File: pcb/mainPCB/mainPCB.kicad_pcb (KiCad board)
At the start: 2 copper layers, 1 part, among them U1 ESP32-S3-DevKitC

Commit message: oskur, cette personne fait sûrement n'imp mais ne s'en aperçois même pas (découvrez son histoire)
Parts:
- added J1: Conn_01x30, Chris:FPC_30_Dell_0.8mm_no0, F.Cu at (102.0, 156.8)
- added J2: Conn_02x15_Counter_Clockwise, Connector_PinHeader_2.54mm:PinHeader_2x15_P2.54mm_Vertical, F.Cu at (84.4, 141.7)
- moved U1 52.6 mm to (149.1, 57.9)
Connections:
- U1 pad 5: unconnected-(U1-GPIO5/ADC1_CH4-Pad5) -> Net-(J1-Pin_14)

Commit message: wip: starting pcb wiring
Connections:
- net Net-(J1-Pin_10) renamed P10
- net Net-(J1-Pin_11) renamed P11
- net Net-(J1-Pin_12) renamed P12
- net Net-(J1-Pin_13) renamed P13
- net Net-(J1-Pin_15) renamed P15
- net Net-(J1-Pin_16) renamed P16
- net Net-(J1-Pin_17) renamed P17
- net Net-(J1-Pin_18) renamed P18
- net Net-(J1-Pin_19) renamed P19
- net Net-(J1-Pin_2) renamed P02
- net Net-(J1-Pin_20) renamed P20
- net Net-(J1-Pin_21) renamed P21
- net Net-(J1-Pin_22) renamed P22
- net Net-(J1-Pin_23) renamed P23
- net Net-(J1-Pin_24) renamed P24
- net Net-(J1-Pin_25) renamed P25
- net Net-(J1-Pin_26) renamed P26
- net Net-(J1-Pin_27) renamed P27
- net Net-(J1-Pin_28) renamed P28
- net Net-(J1-Pin_29) renamed P29
- net Net-(J1-Pin_3) renamed P03
- net Net-(J1-Pin_30) renamed P30
- net Net-(J1-Pin_4) renamed P04
- net Net-(J1-Pin_5) renamed P05
- net Net-(J1-Pin_6) renamed P06
- net Net-(J1-Pin_7) renamed P07
- net Net-(J1-Pin_8) renamed P08
- net Net-(J1-Pin_9) renamed P09
- J1 pad 1: Net-(J1-Pin_1) -> P01
- J1 pad 14: Net-(J1-Pin_14) -> P14
- J2 pad 1: Net-(J1-Pin_1) -> P01
- J2 pad 14: Net-(J1-Pin_14) -> P14
- U1 pad 22: Net-(U1-GND-Pad22) -> P01
- U1 pad 23: Net-(U1-GND-Pad22) -> P01
- U1 pad 24: Net-(U1-GND-Pad22) -> P01
- U1 pad 44: Net-(U1-GND-Pad22) -> P01
- U1 pad 5: Net-(J1-Pin_14) -> unconnected-(U1-GPIO5/ADC1_CH4-Pad5)

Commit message: wip: starting no crossing cable
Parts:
- added R1: 220, Resistor_THT:R_Axial_DIN0207_L6.3mm_D2.5mm_P10.16mm_Horizontal, F.Cu at (161.0, 116.8)
- moved J1 73.4 mm to (125.2, 87.2)
- moved J2 72.9 mm to (106.0, 72.1)
- moved U1 25.1 mm to (156.5, 81.9), turned to 90 degrees
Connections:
- net P01 renamed P01_GND
- net P02 renamed P02_unused
- net P03 renamed P03_unused
- net P04 renamed P04_CAP_LED
- net P05 renamed P05_O10
- net P06 renamed P06_O11
- net P07 renamed P07_O9
- net P08 renamed P08_O14
- net P09 renamed P09_O13
- net P10 renamed P10_O15
- net P11 renamed P11_O16
- net P12 renamed P12_O12
- net P13 renamed P13_O0
- net P14 renamed P14_O2
- net P15 renamed P15_O1
- net P16 renamed P16_O3
- net P17 renamed P17_O8
- net P18 renamed P18_O6
- net P19 renamed P19_O7
- net P20 renamed P20_O4
- net P21 renamed P21_O5
- net P23 renamed P23_I3
- net P25 renamed P25_I5
- net P27 renamed P27_I4
- net P29 renamed P29_I7
- net P30 renamed P30_unused_kb_det
- J1 pad 22: P22 -> P22_I0
- J1 pad 24: P24 -> P24_I1
- J1 pad 26: P26 -> P26_I2
- J1 pad 28: P28 -> P28_I6
- J2 pad 22: P22 -> P22_I0
- J2 pad 24: P24 -> P24_I1
- J2 pad 26: P26 -> P26_I2
- J2 pad 28: P28 -> P28_I6
- U1 pad 27: unconnected-(U1-GPIO21-Pad27) -> Net-(U1-GPIO21)
- U1 pad 38: unconnected-(U1-GPIO41/MTDI-Pad38) -> P22_I0
- U1 pad 39: unconnected-(U1-GPIO42/MTMS-Pad39) -> P24_I1
- U1 pad 40: unconnected-(U1-GPIO2/ADC1_CH1-Pad40) -> P26_I2
- U1 pad 41: unconnected-(U1-GPIO1/ADC1_CH0-Pad41) -> P28_I6

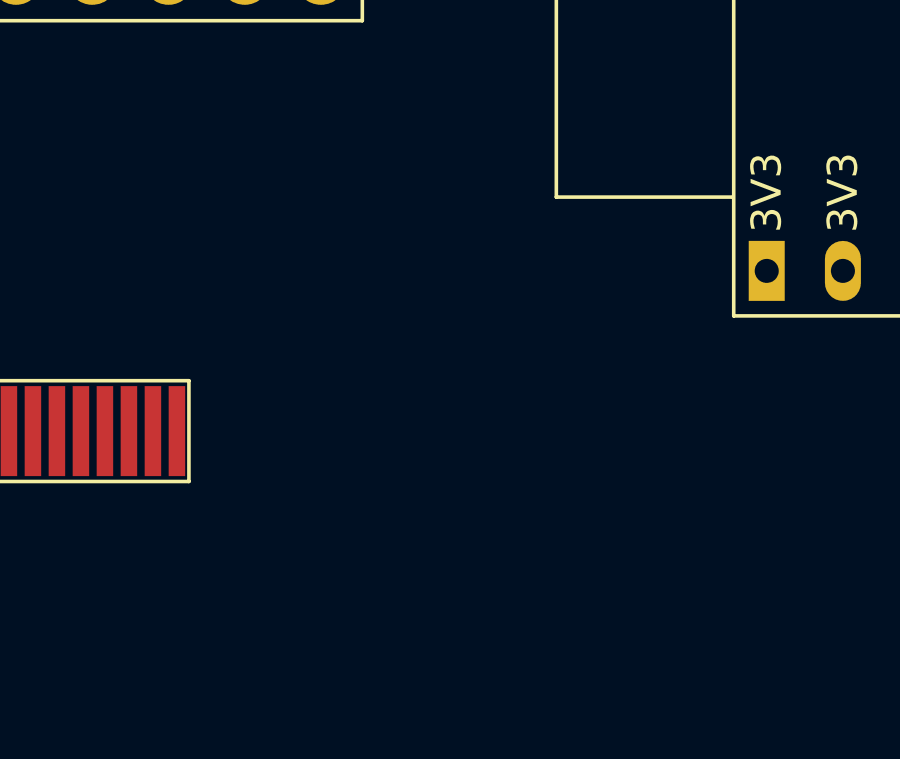
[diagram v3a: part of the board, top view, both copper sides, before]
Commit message: chore: adding backlight connectors
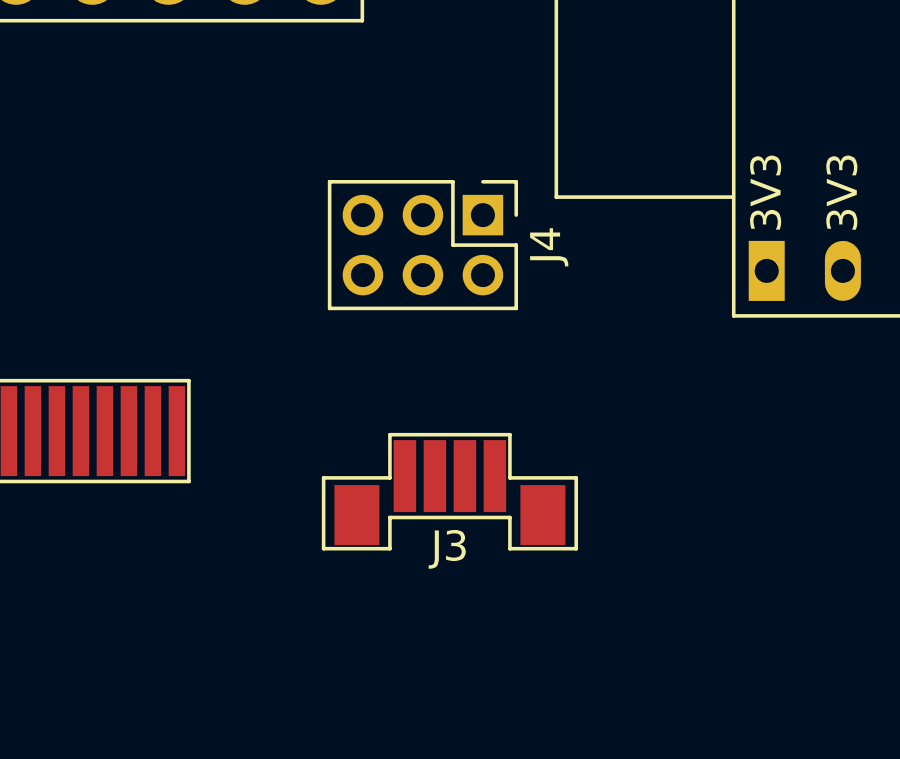
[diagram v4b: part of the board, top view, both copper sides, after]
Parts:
- added J3: Conn_01x04_Shielded_Backlight, Chris:FPC_4_Dell_1mm_with0, F.Cu at (145.9, 88.7)
- added J4: Conn_02x03_Odd_Even_Backlight, Connector_PinHeader_2.00mm:PinHeader_2x03_P2.00mm_Vertical, F.Cu at (147.0, 80.0)

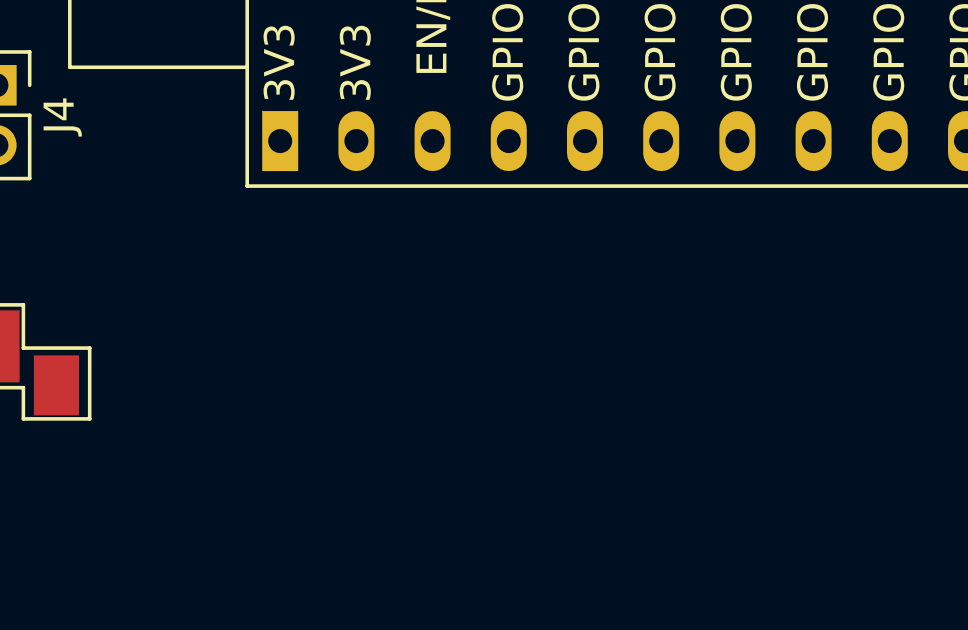
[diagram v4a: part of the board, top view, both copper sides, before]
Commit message: feat: adding NPN for caps led
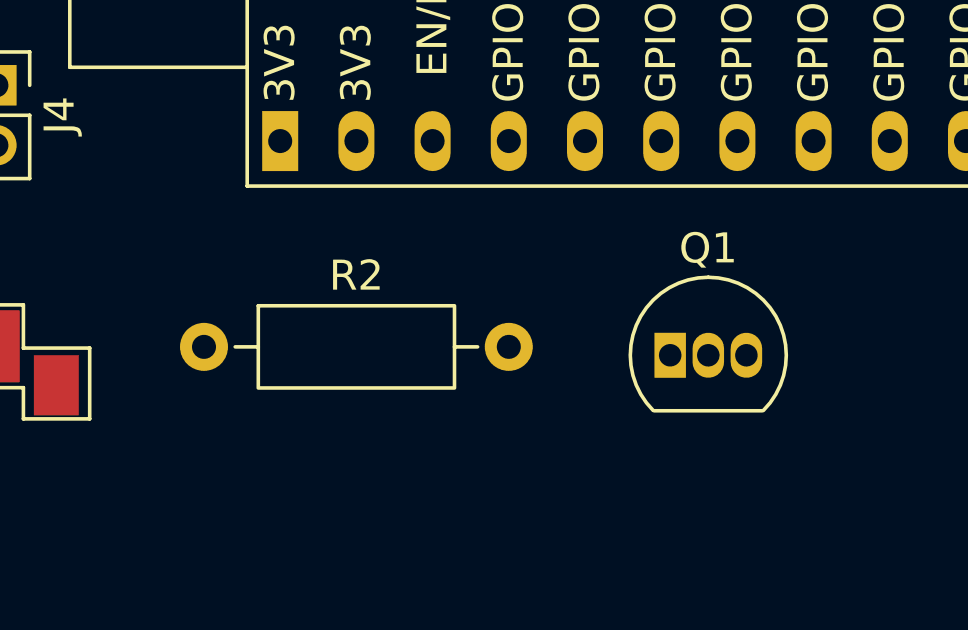
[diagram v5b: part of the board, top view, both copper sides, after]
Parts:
- added Q1: BC547, Package_TO_SOT_THT:TO-92_Inline, F.Cu at (169.5, 89.0)
- added R2: 220, Resistor_THT:R_Axial_DIN0207_L6.3mm_D2.5mm_P10.16mm_Horizontal, F.Cu at (153.9, 88.7)
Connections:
- net Net-(U1-3V3-Pad1) renamed 3_3V
- J3 pad 1: Net-(J3-Pin_1) -> P01_GND
- J4 pad 2: Net-(J3-Pin_1) -> P01_GND
- R1 pad 2: Net-(U1-GPIO21) -> Net-(Q1-E)
- U1 pad 27: Net-(U1-GPIO21) -> unconnected-(U1-GPIO21-Pad27)
- U1 pad 32: unconnected-(U1-GPIO35-Pad32) -> P14_O2
- U1 pad 33: unconnected-(U1-GPIO36-Pad33) -> P14_O2
- U1 pad 34: unconnected-(U1-GPIO37-Pad34) -> P16_O3
- U1 pad 35: unconnected-(U1-GPIO38-Pad35) -> P18_O6
- U1 pad 37: unconnected-(U1-GPIO40/MTDO-Pad37) -> P20_O4

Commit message: chore: more cables
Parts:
- J1: value Conn_01x30 -> Conn_01x30_Keyboard
- moved R1 63.1 mm to (129.8, 62.0)
- moved Q1 37.5 mm to (143.5, 62.0)
- moved U1 1.18 mm to (155.7, 81.0)
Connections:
- U1 pad 10: unconnected-(U1-GPIO17/ADC2_CH6-Pad10) -> P13_O0
- U1 pad 11: unconnected-(U1-GPIO18/ADC2_CH7-Pad11) -> P15_O1
- U1 pad 12: unconnected-(U1-GPIO8/ADC1_CH7-Pad12) -> P17_O8
- U1 pad 4: unconnected-(U1-GPIO4/ADC1_CH3-Pad4) -> CMD_CAP_LED
- U1 pad 5: unconnected-(U1-GPIO5/ADC1_CH4-Pad5) -> P05_O10
- U1 pad 6: unconnected-(U1-GPIO6/ADC1_CH5-Pad6) -> P07_O9
- U1 pad 7: unconnected-(U1-GPIO7/ADC1_CH6-Pad7) -> P09_O13
- U1 pad 8: unconnected-(U1-GPIO15/ADC2_CH4/32K_P-Pad8) -> P09_O13
- U1 pad 9: unconnected-(U1-GPIO16/ADC2_CH5/32K_N-Pad9) -> P11_O16
